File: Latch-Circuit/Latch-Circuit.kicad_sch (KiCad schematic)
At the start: 81 parts, among them J1 SM02B-PASS-1-TB, J10 SM02B-PASS-1-TB, J2 VH_2pin_Side, J3 SM02B-PASS-1-TB, J4 SM03B-PASS-1-TB, J5 SM02B-PASS-1-TB, J6 SM02B-PASS-1-TB, J7 SM02B-PASS-1-TB, J8 SM02B-PASS-1-TB, J9 SM02B-PASS-1-TB, K1 G5Q-1A4_DC12, K2 G5Q-1A4_DC12, K3 G5Q-1A4_DC12, Q1 2N7002K-AU, Q10 2N7002K-AU, Q11 PJA3439-AU_R1_000A1, Q12 2N7002K-AU, Q13 PJA3439-AU_R1_000A1, Q2 PJA3439-AU_R1_000A1, Q3 DMP3098LQ-7, Q4 2N7002K-AU, Q5 2N7002K-AU, Q6 PJA3439-AU_R1_000A1, Q7 2N7002K-AU, Q8 PJA3439-AU_R1_000A1, Q9 PJA3439-AU_R1_000A1

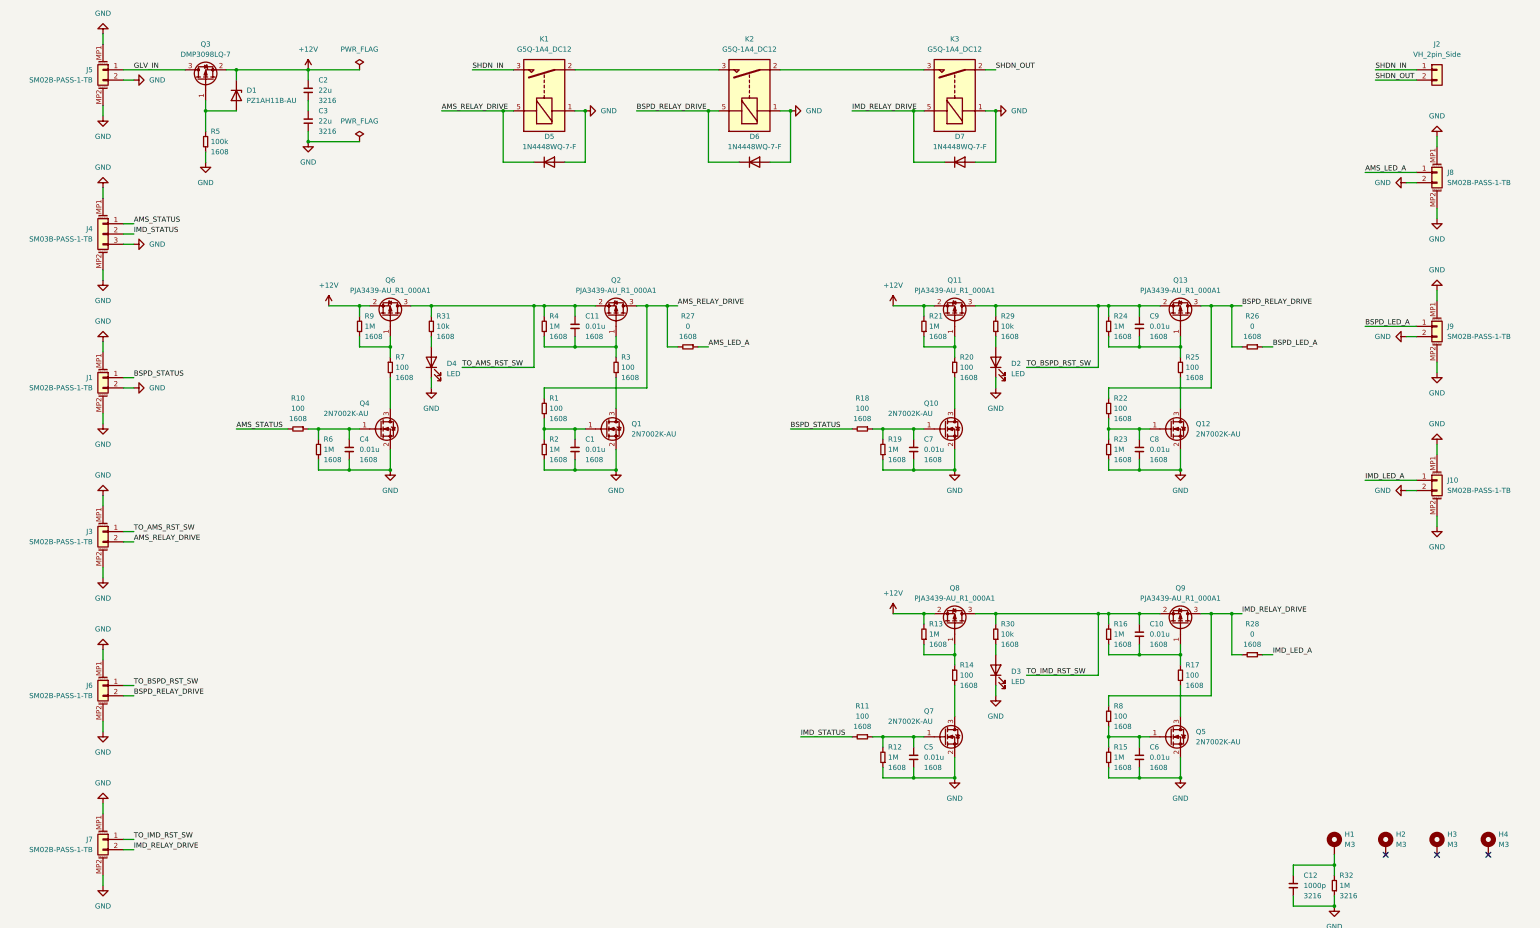
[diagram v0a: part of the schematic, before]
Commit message: コネクタをトップ型に変更、アノテーション、素子配置
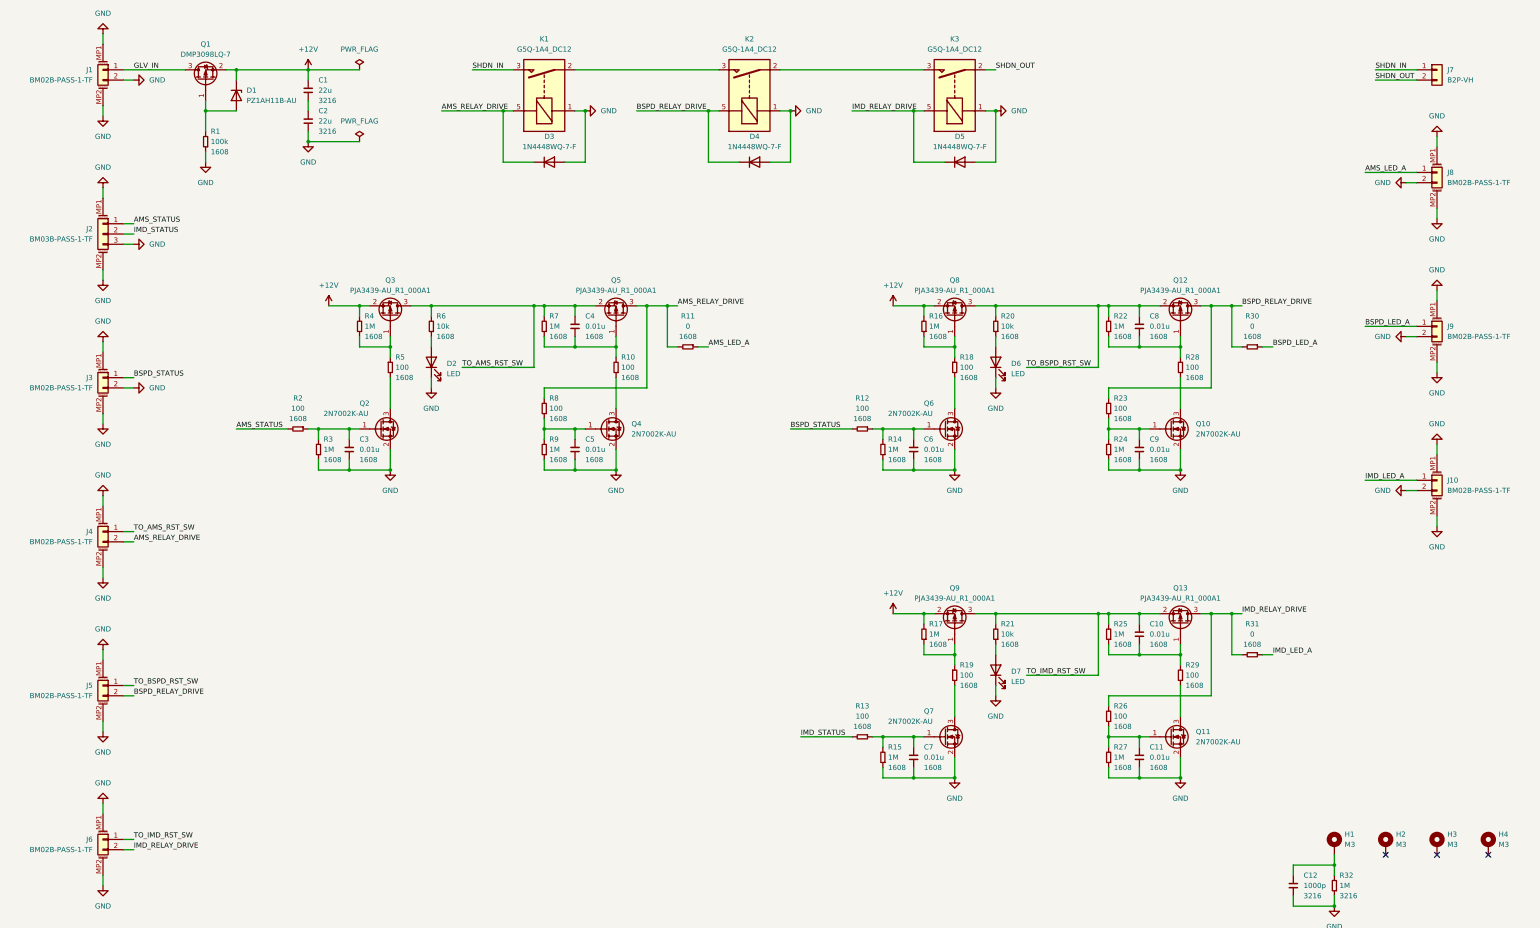
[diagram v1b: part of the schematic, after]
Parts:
- removed J1, J10, J3, J5, J6, J7, J8, J9: SM02B-PASS-1-TB, ProjectEV:Connector_SM02B-PASS-1-TB, symbol ProjectEV:Connector_SM02B-PASS-1-TB
- removed J2: VH_2pin_Side, ProjectEV:Connector_S2P-VH, symbol ProjectEV:Connector_VH_2pin_Side
- removed J4: SM03B-PASS-1-TB, ProjectEV:Connector_SM03B-PASS-1-TB, symbol ProjectEV:Connector_SM03B-PASS-1-TB
- added J1, J10, J3, J4, J5, J6, J8, J9: BM02B-PASS-1-TF, ProjectEV:Connector_BM02B-PASS-1-TF, symbol ProjectEV:Connector_BM02B-PASS-1-TF
- added J2: BM03B-PASS-1-TF, ProjectEV:Connector_BM03B-PASS-1-TF, symbol ProjectEV:Connector_BM03B-PASS-1-TF
- added J7: B2P-VH, ProjectEV:Connector_B2P-VH, symbol ProjectEV:Connector_B2P-VH
- renumbered C2 to C1, C6 to C11, C3 to C2, C4 to C3, C11 to C4, C1 to C5, C7 to C6, C5 to C7, C9 to C8, C8 to C9, D4 to D2, D5 to D3, D6 to D4, D7 to D5, D2 to D6, D3 to D7, Q3 to Q1, Q12 to Q10, Q5 to Q11, Q13 to Q12, Q9 to Q13, Q4 to Q2, Q6 to Q3, Q1 to Q4, Q2 to Q5, Q10 to Q6, Q11 to Q8, Q8 to Q9, R5 to R1, R3 to R10, R27 to R11, R18 to R12, R11 to R13, R19 to R14, R12 to R15, R21 to R16, R13 to R17, R20 to R18, R14 to R19, R10 to R2, R29 to R20, R30 to R21, R24 to R22, R22 to R23, R23 to R24, R16 to R25, R8 to R26, R15 to R27, R25 to R28, R17 to R29, R6 to R3, R26 to R30, R28 to R31, R9 to R4, R7 to R5, R31 to R6, R4 to R7, R1 to R8, R2 to R9
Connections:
- net AMS_LED_A: now also J8.1 (Pin_1)
- net AMS_RELAY_DRIVE: now also J4.2 (Pin_2)
- net AMS_STATUS: now also J2.1 (Pin_1)
- net BSPD_LED_A: now also J9.1 (Pin_1)
- net BSPD_RELAY_DRIVE: now also J5.2 (Pin_2)
- net BSPD_STATUS: now also J3.1 (Pin_1)
- net GLV_IN: now also J1.1 (Pin_1)
- net GND: now also J1.2 (Pin_2), J1.MP1 (MountPin), J1.MP2 (MountPin), J10.2 (Pin_2), J10.MP1 (MountPin), J10.MP2 (MountPin), J2.3 (Pin_3), J2.MP1 (MountPin), J2.MP2 (MountPin), J3.2 (Pin_2), J3.MP1 (MountPin), J3.MP2 (MountPin), J4.MP1 (MountPin), J4.MP2 (MountPin), J5.MP1 (MountPin), J5.MP2 (MountPin), J6.MP1 (MountPin), J6.MP2 (MountPin), J8.2 (Pin_2), J8.MP1 (MountPin), J8.MP2 (MountPin), J9.2 (Pin_2), J9.MP1 (MountPin), J9.MP2 (MountPin)
- net IMD_LED_A: now also J10.1 (Pin_1)
- net IMD_RELAY_DRIVE: now also J6.2 (Pin_2)
- net IMD_STATUS: now also J2.2 (Pin_2)
- net SHDN_IN: now also J7.1 (Pin_1)
- net SHDN_OUT: now also J7.2 (Pin_2)
- net TO_AMS_RST_SW: now also J4.1 (Pin_1)
- net TO_BSPD_RST_SW: now also J5.1 (Pin_1)
- net TO_IMD_RST_SW: now also J6.1 (Pin_1)

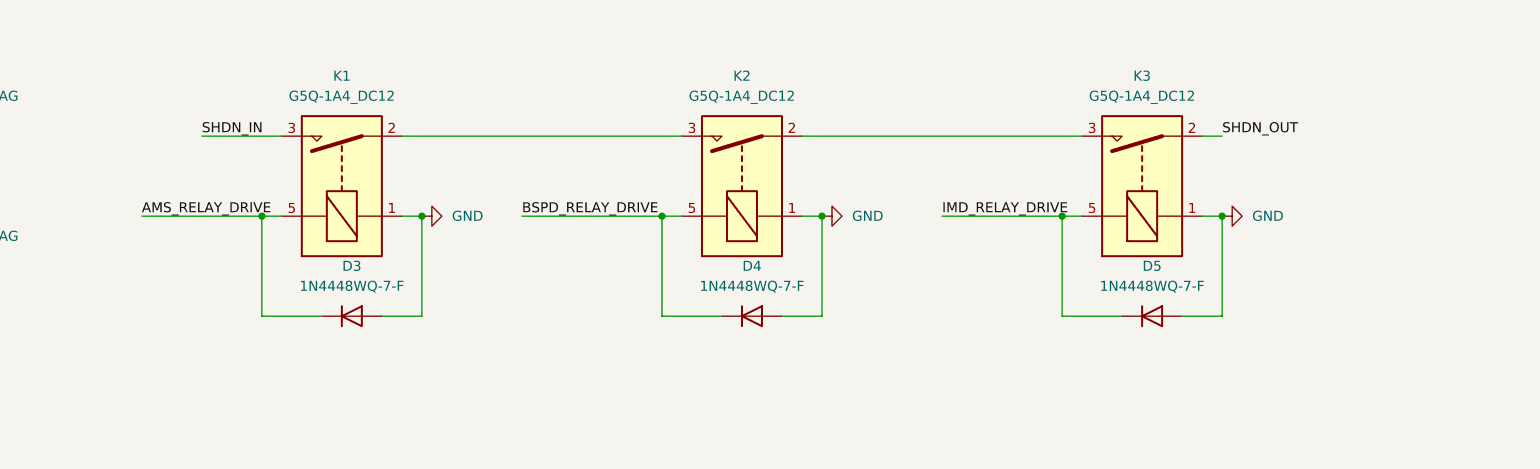
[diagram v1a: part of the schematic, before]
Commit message: 配線完了、リレー配線修正、外周ビア打ち
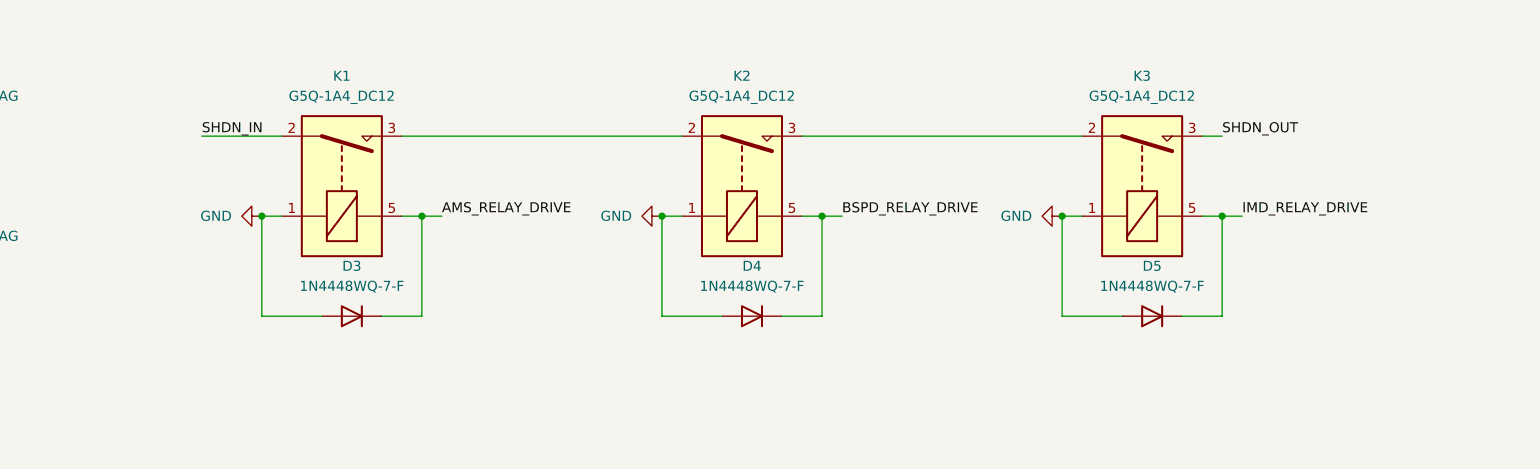
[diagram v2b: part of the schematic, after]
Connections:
- net SHDN_IN: now also K1.2; no longer K1.3
- net SHDN_OUT: now also K3.3; no longer K3.2
- net at K2.2: now also K1.3; no longer K3.3
- net at K2.3: now also K3.2; no longer K1.2
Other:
- moved on the sheet: D3, D4, D5, K1, K2, K3

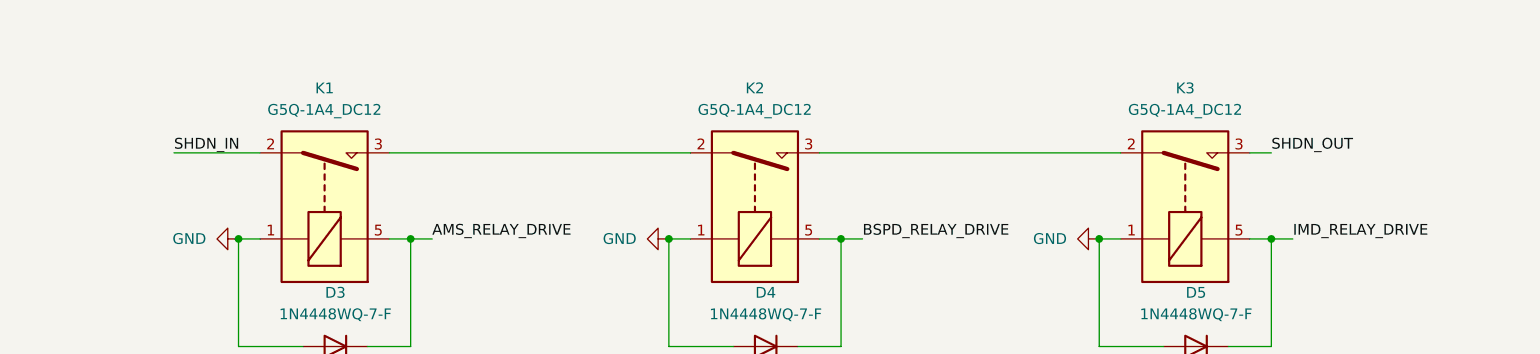
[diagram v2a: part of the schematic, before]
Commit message: シャットダウンチェック用のTP追加
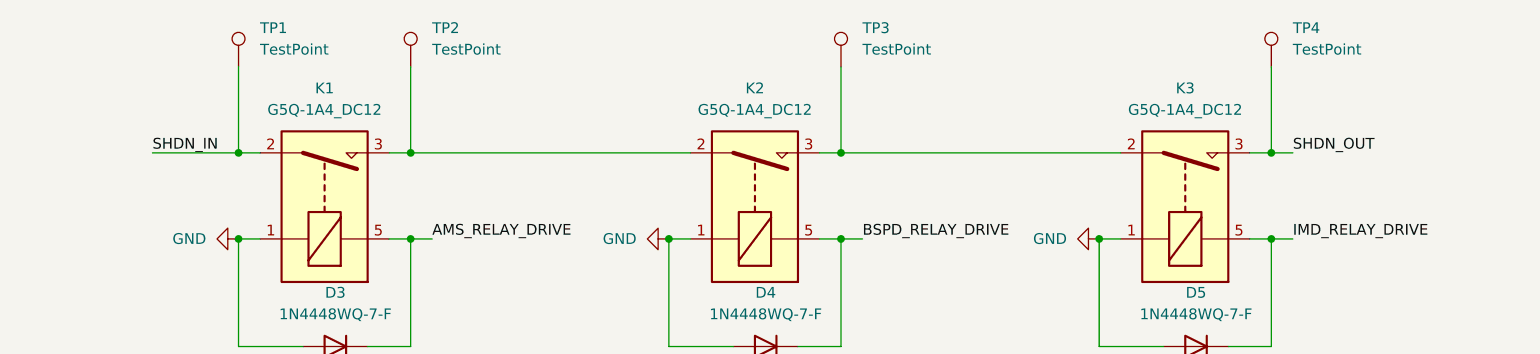
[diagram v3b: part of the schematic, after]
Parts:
- added TP1, TP2, TP3, TP4: TestPoint, TestPoint:TestPoint_Pad_D1.5mm, symbol Connector:TestPoint
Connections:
- net SHDN_IN: now also TP1.1
- net SHDN_OUT: now also TP4.1
- net at K1.3, K2.2: now also TP2.1
- net at K2.3, K3.2: now also TP3.1
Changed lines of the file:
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@@
   (junction (at 294.64 203.2) (diameter 0) (color 0 0 0 0)
   )
+  (junction (at 157.48 38.1) (diameter 0) (color 0 0 0 0)
+  )
   (junction (at 63.5 48.26) (diameter 0) (color 0 0 0 0)
   )
+  (junction (at 259.08 38.1) (diameter 0) (color 0 0 0 0)
+  )
   (junction (at 259.08 172.72) (diameter 0) (color 0 0 0 0)
   )
@@
   (junction (at 294.64 96.52) (diameter 0) (color 0 0 0 0)
   )
+  (junction (at 208.28 38.1) (diameter 0) (color 0 0 0 0)
+  )
   (junction (at 109.22 106.68) (diameter 0) (color 0 0 0 0)
   )
@@
   (junction (at 248.92 182.88) (diameter 0) (color 0 0 0 0)
   )
+  (junction (at 137.16 38.1) (diameter 0) (color 0 0 0 0)
+  )
   (junction (at 177.8 96.52) (diameter 0) (color 0 0 0 0)
   )
@@
     (stroke (width 0) (type default))
   )
+  (wire (pts (xy 157.48 27.94) (xy 157.48 38.1))
+    (stroke (width 0) (type default))
+  )
   (wire (pts (xy 152.4 60.96) (xy 157.48 60.96))
     (stroke (width 0) (type default))
@@
     (stroke (width 0) (type default))
   )
+  (wire (pts (xy 208.28 27.94) (xy 208.28 38.1))
+    (stroke (width 0) (type default))
+  )
   (wire (pts (xy 119.38 104.14) (xy 119.38 106.68))
     (stroke (width 0) (type default))
@@
     (stroke (width 0) (type default))
   )
+  (wire (pts (xy 157.48 38.1) (xy 190.5 38.1))
+    (stroke (width 0) (type default))
+  )
   (wire (pts (xy 238.76 127) (xy 241.3 127))
     (stroke (width 0) (type default))
@@
     (stroke (width 0) (type default))
   )
-  (wire (pts (xy 154.94 38.1) (xy 190.5 38.1))
+  (wire (pts (xy 154.94 38.1) (xy 157.48 38.1))
     (stroke (width 0) (type default))
   )
@@
     (stroke (width 0) (type default))
   )
+  (wire (pts (xy 256.54 38.1) (xy 259.08 38.1))
+    (stroke (width 0) (type default))
+  )
+  (wire (pts (xy 208.28 38.1) (xy 241.3 38.1))
+    (stroke (width 0) (type default))
+  )
   (wire (pts (xy 137.16 48.26) (xy 139.7 48.26))
     (stroke (width 0) (type default))
@@
     (stroke (width 0) (type default))
   )
-  (wire (pts (xy 205.74 38.1) (xy 241.3 38.1))
+  (wire (pts (xy 137.16 38.1) (xy 139.7 38.1))
     (stroke (width 0) (type default))
   )
@@
     (stroke (width 0) (type default))
   )
+  (wire (pts (xy 259.08 38.1) (xy 261.62 38.1))
+    (stroke (width 0) (type default))
+  )
   (wire (pts (xy 88.9 53.34) (xy 88.9 55.88))
     (stroke (width 0) (type default))
@@
     (stroke (width 0) (type default))
   )
+  (wire (pts (xy 137.16 27.94) (xy 137.16 38.1))
+    (stroke (width 0) (type default))
+  )
   (wire (pts (xy 231.14 210.82) (xy 231.14 213.36))
     (stroke (width 0) (type default))
@@
     (stroke (width 0) (type default))
   )
+  (wire (pts (xy 205.74 38.1) (xy 208.28 38.1))
+    (stroke (width 0) (type default))
+  )
   (wire (pts (xy 231.14 213.36) (xy 238.76 213.36))
     (stroke (width 0) (type default))
@@
     (stroke (width 0) (type default))
   )
-  (wire (pts (xy 259.08 96.52) (xy 259.08 99.06))
+  (wire (pts (xy 259.08 27.94) (xy 259.08 38.1))
     (stroke (width 0) (type default))
   )
-  (wire (pts (xy 127 111.76) (xy 144.78 111.76))
+  (wire (pts (xy 259.08 96.52) (xy 259.08 99.06))
     (stroke (width 0) (type default))
   )
-  (wire (pts (xy 256.54 38.1) (xy 259.08 38.1))
+  (wire (pts (xy 127 111.76) (xy 144.78 111.76))
     (stroke (width 0) (type default))
   )
@@
     (stroke (width 0) (type default))
   )
-  (wire (pts (xy 129.54 38.1) (xy 139.7 38.1))
+  (wire (pts (xy 127 38.1) (xy 137.16 38.1))
     (stroke (width 0) (type default))
   )
@@
     (effects (font (size 1.27 1.27)) (justify left bottom))
   )
-  (label "SHDN_IN" (at 129.54 38.1 0) (fields_autoplaced)
+  (label "SHDN_IN" (at 127 38.1 0) (fields_autoplaced)
     (effects (font (size 1.27 1.27)) (justify left bottom))
   )
@@
     (effects (font (size 1.27 1.27)) (justify left bottom))
   )
-  (label "SHDN_OUT" (at 259.08 38.1 0) (fields_autoplaced)
+  (label "SHDN_OUT" (at 261.62 38.1 0) (fields_autoplaced)
     (effects (font (size 1.27 1.27)) (justify left bottom))
   )
@@
     (effects (font (size 1.27 1.27)) (justify left bottom))
   )
+  (symbol (lib_id "Connector:TestPoint") (at 137.16 27.94 0) (unit 1)
+    (in_bom yes) (on_board yes) (dnp no) (fields_autoplaced)
+    (property "Reference" "TP1" (at 139.7 23.368 0)
+      (effects (font (size 1.27 1.27)) (justify left))
+    )
+    (property "Value" "TestPoint" (at 139.7 25.908 0)
+      (effects (font (size 1.27 1.27)) (justify left))
+    )
+    (property "Footprint" "TestPoint:TestPoint_Pad_D1.5mm" (at 142.24 27.94 0)
+      (effects (font (size 1.27 1.27)) hide)
+    )
+    (property "Datasheet" "~" (at 142.24 27.94 0)
+      (effects (font (size 1.27 1.27)) hide)
+    )
+    (pin "1")
+    (instances
+      (project "Latch-Circuit"
+        (path "/32b50168-feb5-4f60-b0c0-d9d9b13c9014"
+          (reference "TP1") (unit 1)
+        )
+      )
+    )
+  )
   (symbol (lib_id "ProjectEV:C") (at 154.94 132.08 0) (unit 1)
     (in_bom yes) (on_board yes) (dnp no) (fields_autoplaced)
@@
     )
   )
+  (symbol (lib_id "Connector:TestPoint") (at 157.48 27.94 0) (unit 1)
+    (in_bom yes) (on_board yes) (dnp no) (fields_autoplaced)
+    (property "Reference" "TP2" (at 160.02 23.368 0)
+      (effects (font (size 1.27 1.27)) (justify left))
+    )
+    (property "Value" "TestPoint" (at 160.02 25.908 0)
+      (effects (font (size 1.27 1.27)) (justify left))
+    )
+    (property "Footprint" "TestPoint:TestPoint_Pad_D1.5mm" (at 162.56 27.94 0)
+      (effects (font (size 1.27 1.27)) hide)
+    )
+    (property "Datasheet" "~" (at 162.56 27.94 0)
+      (effects (font (size 1.27 1.27)) hide)
+    )
+    (pin "1")
+    (instances
+      (project "Latch-Circuit"
+        (path "/32b50168-feb5-4f60-b0c0-d9d9b13c9014"
+          (reference "TP2") (unit 1)
+        )
+      )
+    )
+  )
   (symbol (lib_id "Device:LED") (at 119.38 110.49 90) (unit 1)
     (in_bom yes) (on_board yes) (dnp no) (fields_autoplaced)
@@
     )
   )
+  (symbol (lib_id "Connector:TestPoint") (at 208.28 27.94 0) (unit 1)
+    (in_bom yes) (on_board yes) (dnp no) (fields_autoplaced)
+    (property "Reference" "TP3" (at 210.82 23.368 0)
+      (effects (font (size 1.27 1.27)) (justify left))
+    )
+    (property "Value" "TestPoint" (at 210.82 25.908 0)
+      (effects (font (size 1.27 1.27)) (justify left))
+    )
+    (property "Footprint" "TestPoint:TestPoint_Pad_D1.5mm" (at 213.36 27.94 0)
+      (effects (font (size 1.27 1.27)) hide)
+    )
+    (property "Datasheet" "~" (at 213.36 27.94 0)
+      (effects (font (size 1.27 1.27)) hide)
+    )
+    (pin "1")
+    (instances
+      (project "Latch-Circuit"
+        (path "/32b50168-feb5-4f60-b0c0-d9d9b13c9014"
+          (reference "TP3") (unit 1)
+        )
+      )
+    )
+  )
   (symbol (lib_id "ProjectEV:Connector_B2P-VH") (at 368.3 38.1 0) (unit 1)
     (in_bom yes) (on_board yes) (dnp no) (fields_autoplaced)
@@
         )
       )
+    )
+  )
+  (symbol (lib_id "Connector:TestPoint") (at 259.08 27.94 0) (unit 1)
+    (in_bom yes) (on_board yes) (dnp no) (fields_autoplaced)
+    (property "Reference" "TP4" (at 261.62 23.368 0)
+      (effects (font (size 1.27 1.27)) (justify left))
+    )
+    (property "Value" "TestPoint" (at 261.62 25.908 0)
+      (effects (font (size 1.27 1.27)) (justify left))
+    )
+    (property "Footprint" "TestPoint:TestPoint_Pad_D1.5mm" (at 264.16 27.94 0)
+      (effects (font (size 1.27 1.27)) hide)
+    )
+    (property "Datasheet" "~" (at 264.16 27.94 0)
+      (effects (font (size 1.27 1.27)) hide)
+    )
+    (pin "1")
+    (instances
+      (project "Latch-Circuit"
+        (path "/32b50168-feb5-4f60-b0c0-d9d9b13c9014"
+          (reference "TP4") (unit 1)
+        )
+      )

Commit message: コメント追加
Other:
- note added: "AMSのラッチ回路を例に、動作を説明する。 TO_AMS_RST_SW, AMS_RELAY_DRIVE間にはプッシュスイッチが実装される。他2つも同様。 セット動作 LATCH CIRCUITにHIGHが入力されているとき、 プッシュスイッチを押すと一時的にAMS_RELAY_DRIVEがHIGHとなる。 そして、LATCH CIRCUIT下側Nch MOSFETのゲートがHIGHになると、上側Pch MOSFETのゲートがLOWになる。 一度Pch MOSFETをONしてしまえば、AMS_RELAY_DRIVEはPch MOSFETによりHIGHとなるので、ON状態を保持することができる。 リセット動作 LATCH CIRCUITの入力をLOWにすることで、リセットされる。 再び入力がHIGHになったとしても、Pch MOSFETはOFF状態であるため、AMS_RELAY_DRIVE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"
- note added: "HIGH IMPEDANCE INPUT LOW IMPEDANCE OUTPUT"
- note added: "LATCH CIRCUIT"
- note added: "RELAYS of SHUTDOWN CIRCUIT"
- moved on the sheet: C10, C11, C3, C6, C7, C8, C9, D2, D6, D7, Q10, Q11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
